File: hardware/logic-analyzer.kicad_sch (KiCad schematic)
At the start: 93 parts, among them J1 USB_C_Receptacle, J2 Conn_02x20, J3 Conn_02x04, J4 Conn_02x15, SW1 SW_Push, SW2 SW_Push, U1 CH32H417MxUx, U16 TPD4EUSB30, U2 Opamp_Dual, U22 TPD4EUSB30, U23 TPD4EUSB30, U3 CH9441P, U4 XC6206PxxxMR, Y1 25MHz 20pF

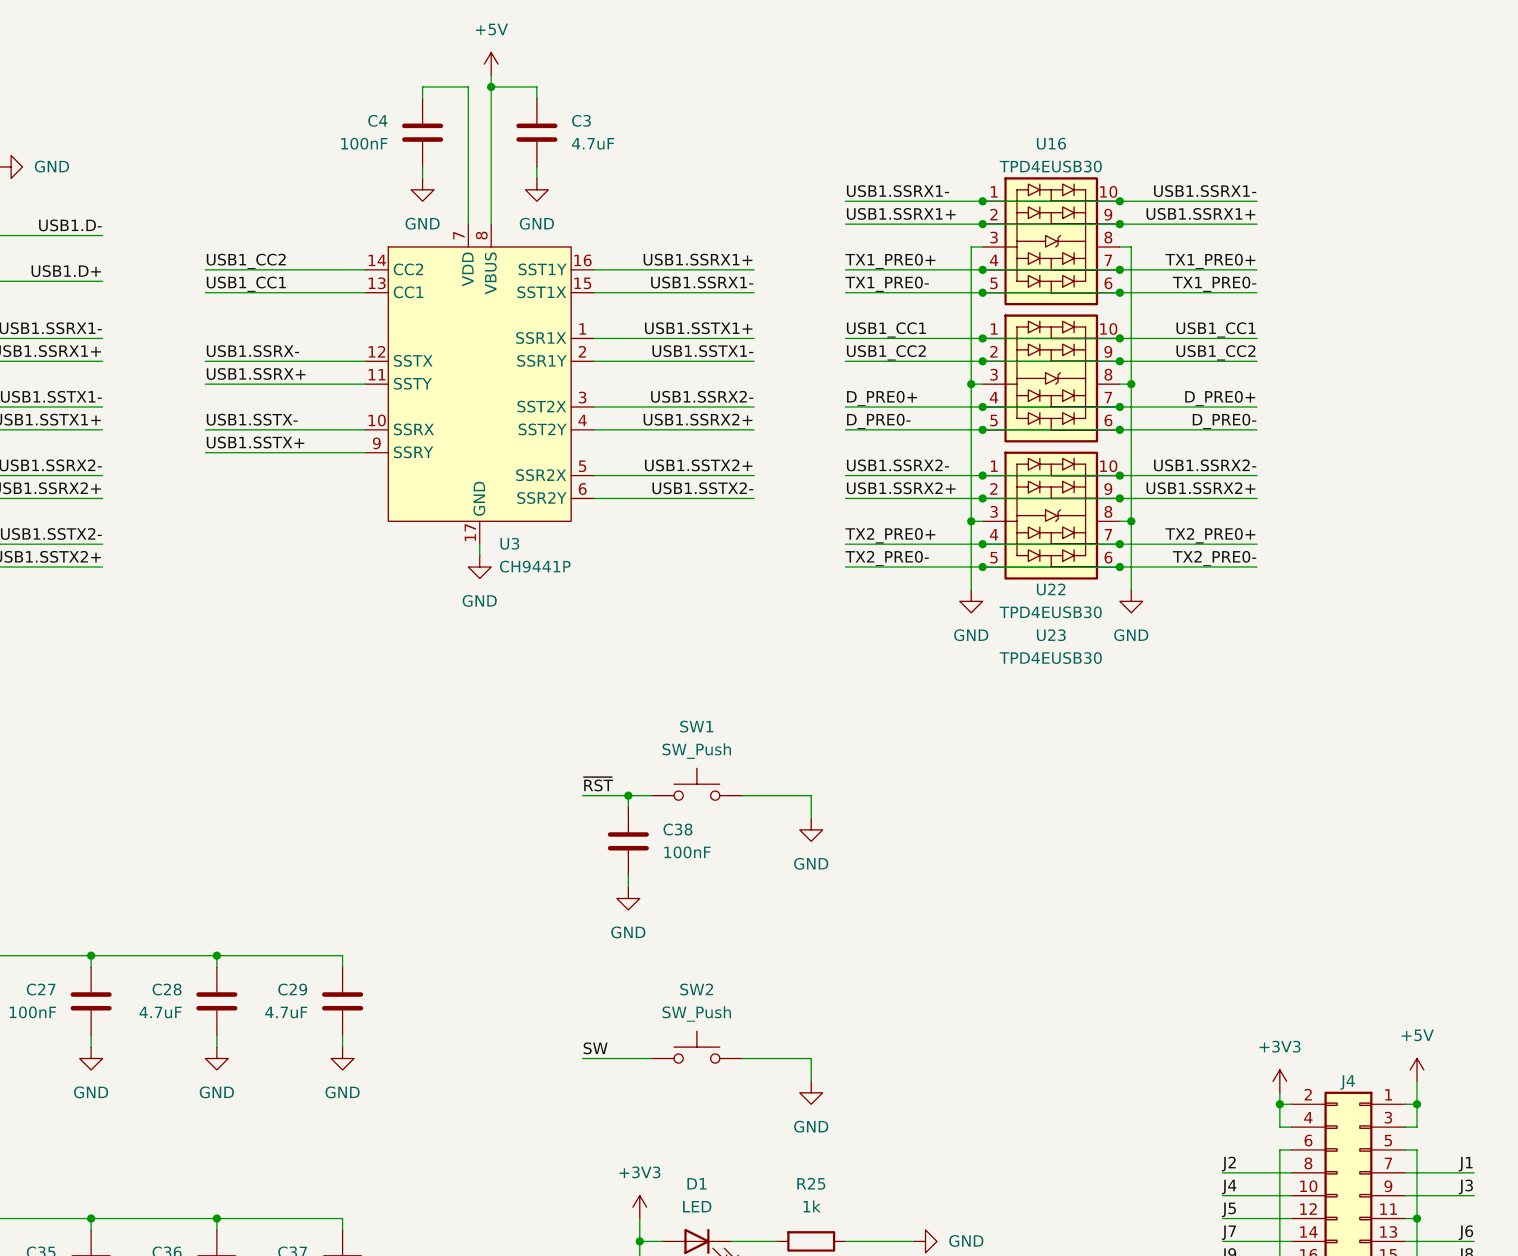
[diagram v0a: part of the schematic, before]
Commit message: Change CH9441P into something available
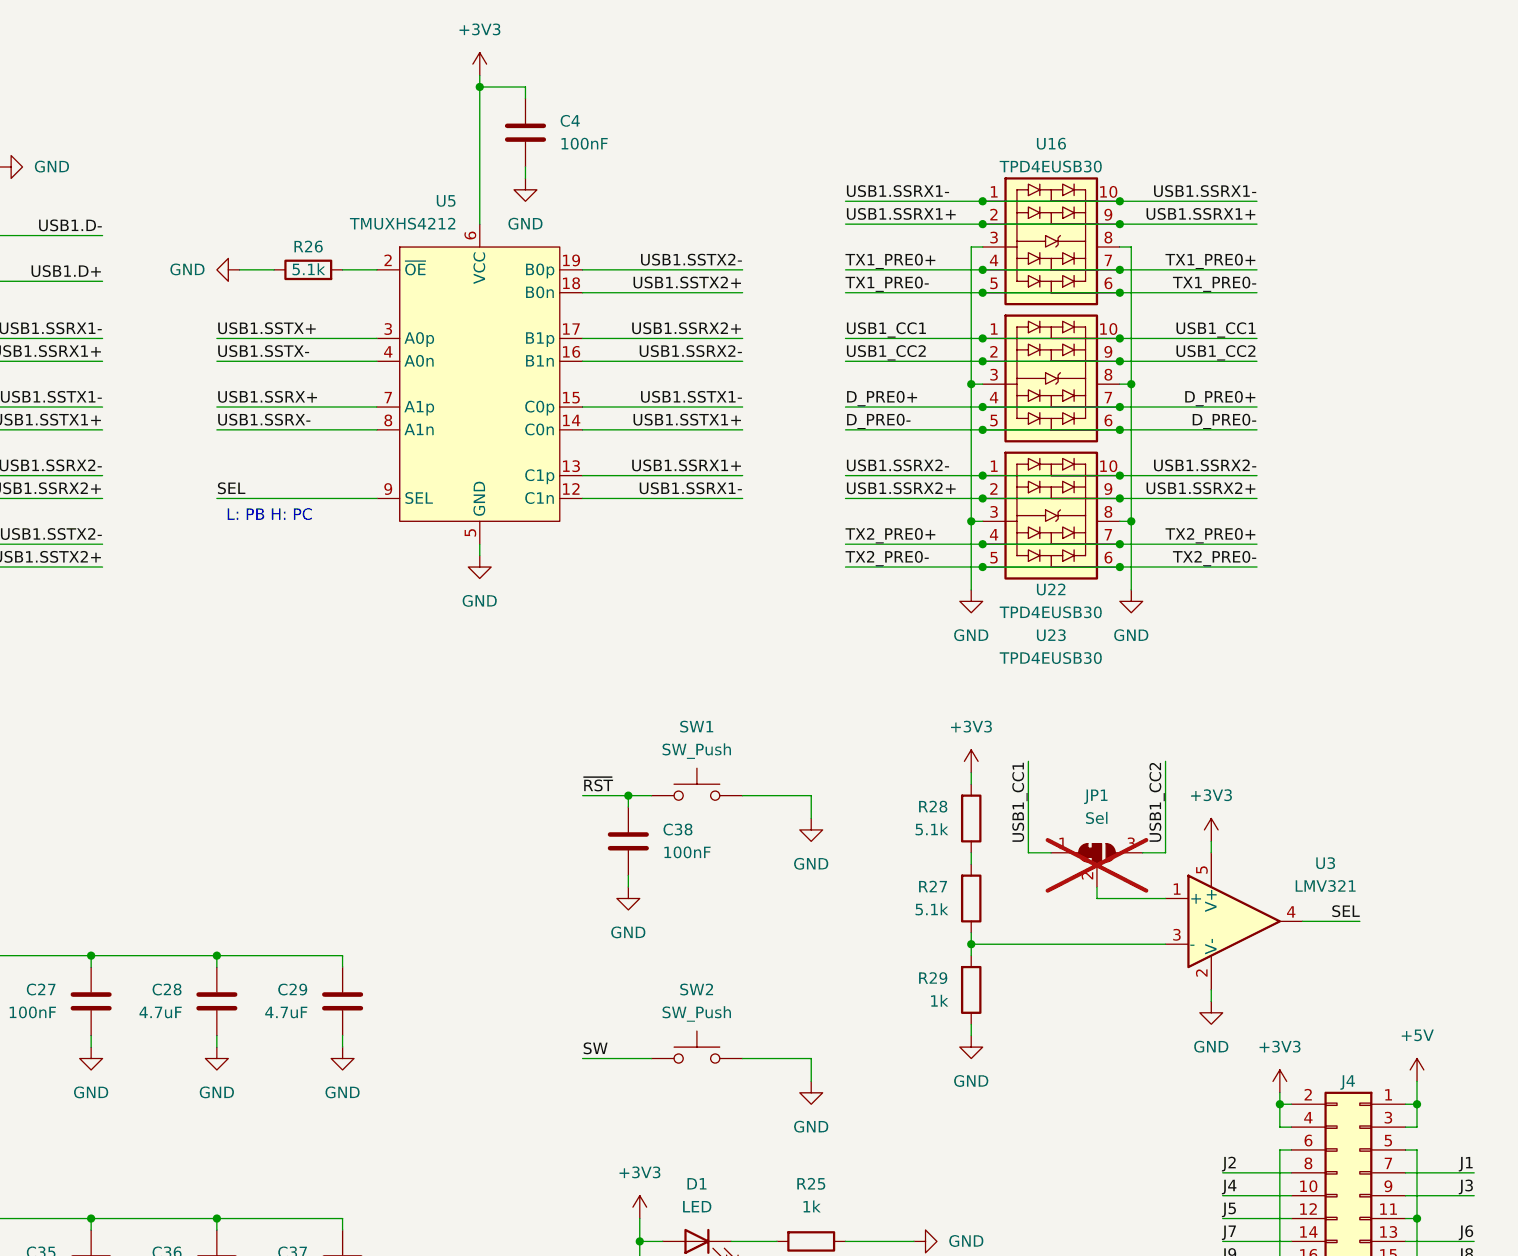
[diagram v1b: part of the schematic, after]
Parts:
- removed C3: 4.7uF, Capacitor_SMD:C_0402_1005Metric, symbol Device:C
- removed U3: CH9441P, Package_DFN_QFN:QFN-16-1EP_3x3mm_P0.5mm_EP1.75x1.75mm_ThermalVias, symbol logic-analyzer:CH9441P
- added JP1: Sel, Jumper:SolderJumper-3_P1.3mm_Bridged12_RoundedPad1.0x1.5mm, symbol Jumper:SolderJumper_3_Bridged12
- added R26, R27, R28: 5.1k, Resistor_SMD:R_0402_1005Metric, symbol Device:R
- added R29: 1k, Resistor_SMD:R_0402_1005Metric, symbol Device:R
- added U3: LMV321, Package_TO_SOT_SMD:SOT-353_SC-70-5, symbol Amplifier_Operational:LMV321
- added U5: TMUXHS4212, Package_DFN_QFN:DHVQFN-20-1EP_2.5x4.5mm_P0.5mm_EP1x3mm, symbol logic-analyzer:TMUXHS4212
- R23, R24, R25: footprint Resistor_SMD:R_0402_1005Metric_Pad0.72x0.64mm_HandSolder -> Resistor_SMD:R_0402_1005Metric
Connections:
- net +3V3: now also C4.1, R28.2, U3.5 (V+), U5.1 (RSVD1), U5.10 (RSVD2), U5.6 (VCC)
- net GND: now also R26.1, R29.1, U3.2 (V-), U5.11 (GND), U5.20 (GND), U5.21 (GND), U5.5 (GND)
- net USB1.SSRX+: now also U5.7 (A1p)
- net USB1.SSRX-: now also U5.8 (A1n)
- net USB1.SSRX1+: now also U5.13 (C1p)
- net USB1.SSRX1-: now also U5.12 (C1n)
- net USB1.SSRX2+: now also U5.17 (B1p)
- net USB1.SSRX2-: now also U5.16 (B1n)
- net USB1.SSTX+: now also U5.3 (A0p)
- net USB1.SSTX-: now also U5.4 (A0n)
- net USB1.SSTX1+: now also U5.14 (C0n)
- net USB1.SSTX1-: now also U5.15 (C0p)
- net USB1.SSTX2+: now also U5.18 (B0n)
- net USB1.SSTX2-: now also U5.19 (B0p)
- net USB1_CC1: now also JP1.1 (A)
- net USB1_CC2: now also JP1.3 (B)
- new net: JP1.2 (C), U3.1 (+)
- new net: R26.2, U5.2 (~{OE})
- new net: R27.2, R28.1
- new net: R27.1, R29.2, U3.3 (-)
- new net SEL: U3.4, U5.9 (SEL)
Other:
- note added: "L: PB H: PC"
- moved on the sheet: C4

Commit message: Readme
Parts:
- added TP1, TP2, TP3, TP4: TestPoint_Probe, TestPoint:TestPoint_Pad_D1.5mm, symbol Connector:TestPoint_Probe
- R18, R19: LCSC Part # C2906860 -> C106232
- R21, R22, R26, R27, R28: LCSC Part # C2906874 -> C105872
- R23, R24, R25, R29: LCSC Part # C2906864 -> C106235
- R97, R98: LCSC Part # C53454336 -> C54920775
- U1: LCSC Part # (none) -> C54973456
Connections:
- net +3V3: now also TP3.1
- net GND: now also TP4.1
- net USB1.D+: now also TP1.1
- net USB1.D-: now also TP2.1

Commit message: Update
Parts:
- removed C22: 100nF, Capacitor_SMD:C_0402_1005Metric, symbol Device:C
- removed R17: 220R, Resistor_SMD:R_0402_1005Metric, symbol Device:R
- removed U2: Opamp_Dual, Package_SO:VSSOP-8_2.3x2mm_P0.5mm, symbol Device:Opamp_Dual
- added R30, R31, R32: 100R, Resistor_SMD:R_0402_1005Metric, symbol Device:R
- C1, C2: MPN (none) -> GCM1555C1H330JA16J
- C10, C11, C12, C13, C14, C15, C16, C17, C18, C19, C20, C5, C6, C7, C8, C9: MPN (none) -> VJ0402A150JXAAC
- C21, C23, C24, C25, C26, C27, C30, C31, C32, C34, C35, C358, C359, C36, C360, C361, C38, C4: LCSC Part # C110251 -> C60474; MPN (none) -> CC0402KRX7R7BB104
- C28, C29, C33, C37, C39, C40: LCSC Part # C7472956 -> C51933306; MPN (none) -> GRM155R60G475ME87D
- D1, D2, D3: LCSC Part # C20613596 -> C51933306
- J2: footprint Connector_PinSocket_1.27mm:PinSocket_2x20_P1.27mm_Horizontal -> Connector_PinHeader_1.27mm:PinHeader_2x20_P1.27mm_Horizontal
- J3: footprint Connector_PinSocket_1.27mm:PinSocket_2x04_P1.27mm_Horizontal -> Connector_PinHeader_1.27mm:PinHeader_2x04_P1.27mm_Horizontal
- R1, R10, R11, R12, R13, R14, R15, R16, R2, R3, R4, R5, R6, R7, R8, R9: LCSC Part # C2906864 -> C106235; MPN (none) -> RC0402FR-071KL
- R18, R19: MPN (none) -> MCS04020C1000FE000
- R20: value 220R -> 100R; LCSC Part # C25091 -> C106232; MPN (none) -> MCS04020C1000FE000
- R21, R22, R26, R27, R28: MPN (none) -> AC0402FR-075K1L
- R23, R24, R25, R29: MPN (none) -> RC0402FR-071KL
- R97, R98: MPN (none) -> RC0402FR-072R2L
- RN1, RN2, RN3, RN4: MPN (none) -> EXB-V8V104JV
- U1: MPN (none) -> CH32H417MEU6
- U16, U22, U23: MPN (none) -> TPD4EUSB30DQAR
- U3: MPN (none) -> LMV321IDCKT
- U4: MPN (none) -> XC6206P332MR-G
- U5: MPN (none) -> TMUXHS4212RKSR
- Y1: LCSC Part # C252274 -> C37635326; MPN (none) -> XT1220HJRGX25M00E
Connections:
- net +1V8: now also J2.27 (Pin_27), J2.37 (Pin_37); no longer J2.13 (Pin_13), J2.3 (Pin_3)
- net +3V3: now also J2.17 (Pin_17), J2.7 (Pin_7); no longer J2.23 (Pin_23), J2.33 (Pin_33)
- net +5V: no longer J4.3 (Pin_3)
- net A0: now also R18.2, R30.1
- net A1: now also R19.2, R20.1
- net ACH0: now also J3.6 (Pin_6); no longer J3.4 (Pin_4)
- net ACH1: now also J3.2 (Pin_2); no longer J3.8 (Pin_8)
- net CH0: now also J2.38 (Pin_38); no longer J2.4 (Pin_4)
- net CH1: now also J2.36 (Pin_36); no longer J2.6 (Pin_6)
- net CH10: now also J2.14 (Pin_14); no longer J2.28 (Pin_28)
- net CH11: now also J2.12 (Pin_12); no longer J2.30 (Pin_30)
- net CH12: now also J2.8 (Pin_8); no longer J2.34 (Pin_34)
- net CH13: now also J2.6 (Pin_6); no longer J2.36 (Pin_36)
- net CH14: now also J2.4 (Pin_4); no longer J2.38 (Pin_38)
- net CH15: now also J2.2 (Pin_2); no longer J2.40 (Pin_40)
- net CH2: now also J2.34 (Pin_34); no longer J2.8 (Pin_8)
- net CH3: now also J2.32 (Pin_32); no longer J2.10 (Pin_10)
- net CH4: now also J2.28 (Pin_28); no longer J2.14 (Pin_14)
- net CH5: now also J2.26 (Pin_26); no longer J2.16 (Pin_16)
- net CH6: now also J2.24 (Pin_24); no longer J2.18 (Pin_18)
- net CH7: now also J2.22 (Pin_22); no longer J2.20 (Pin_20)
- net CH8: now also J2.18 (Pin_18); no longer J2.24 (Pin_24)
- net CH9: now also J2.16 (Pin_16); no longer J2.26 (Pin_26)
- net GND: now also J2.10 (Pin_10), J2.13 (Pin_13), J2.20 (Pin_20), J2.23 (Pin_23), J2.3 (Pin_3), J2.30 (Pin_30), J2.33 (Pin_33), J2.40 (Pin_40), J3.4 (Pin_4), J3.8 (Pin_8), R31.2, R32.2; no longer J2.12 (Pin_12), J2.17 (Pin_17), J2.2 (Pin_2), J2.22 (Pin_22), J2.27 (Pin_27), J2.32 (Pin_32), J2.37 (Pin_37), J2.7 (Pin_7), J3.2 (Pin_2), J3.6 (Pin_6), J4.5 (Pin_5), R20.2
- net USB1.D+: now also J4.3 (Pin_3)
- net USB1.D-: now also J4.5 (Pin_5)
- new net: R20.2, R32.1
- new net: R30.2, R31.1
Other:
- moved on the sheet: R18, R19

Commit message: Stencil
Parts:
- added H1, H2: MountingHole, logic-analyzer:Icy Electronics Logo, symbol Mechanical:MountingHole
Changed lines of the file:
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@@
 	)
 	(symbol
+		(lib_id "Mechanical:MountingHole")
+		(at 400.05 260.35 0)
+		(unit 1)
+		(body_style 1)
+		(exclude_from_sim no)
+		(in_bom no)
+		(on_board yes)
+		(in_pos_files yes)
+		(dnp no)
+		(fields_autoplaced yes)
+		(property "Reference" "H1"
+			(at 402.59 259.0799 0)
+			(hide yes)
+			(show_name no)
+			(do_not_autoplace no)
+			(effects
+				(font
+					(size 1.27 1.27)
+				)
+				(justify left)
+			)
+		)
+		(property "Value" "MountingHole"
+			(at 402.59 261.6199 0)
+			(hide yes)
+			(show_name no)
+			(do_not_autoplace no)
+			(effects
+				(font
+					(size 1.27 1.27)
+				)
+				(justify left)
+			)
+		)
+		(property "Footprint" "logic-analyzer:Icy Electronics Logo"
+			(at 400.05 260.35 0)
+			(hide yes)
+			(show_name no)
+			(do_not_autoplace no)
+			(effects
+				(font
+					(size 1.27 1.27)
+				)
+			)
+		)
+		(property "Datasheet" ""
+			(at 400.05 260.35 0)
+			(hide yes)
+			(show_name no)
+			(do_not_autoplace no)
+			(effects
+				(font
+					(size 1.27 1.27)
+				)
+			)
+		)
+		(property "Description" "Mounting Hole without connection"
+			(at 400.05 260.35 0)
+			(hide yes)
+			(show_name no)
+			(do_not_autoplace no)
+			(effects
+				(font
+					(size 1.27 1.27)
+				)
+			)
+		)
+		(instances
+			(project "logic-analyzer"
+				(path "/5f684d88-c692-47c7-8c9f-30135288a837"
+					(reference "H1")
+					(unit 1)
+				)
+			)
+		)
+	)
+	(symbol
 		(lib_id "power:GND")
 		(at 185.42 133.35 0)
@@
 					(unit 1)
 				)
+			)
+		)
+	)
+	(symbol
+		(lib_id "Mechanical:MountingHole")
+		(at 391.16 260.35 0)
+		(unit 1)
+		(body_style 1)
+		(exclude_from_sim no)
+		(in_bom no)
+		(on_board yes)
+		(in_pos_files yes)
+		(dnp no)
+		(fields_autoplaced yes)
+		(property "Reference" "H2"
+			(at 393.7 259.0799 0)
+			(hide yes)
+			(show_name no)
+			(do_not_autoplace no)
+			(effects
+				(font
+					(size 1.27 1.27)
+				)
+				(justify left)
+			)
+		)
+		(property "Value" "MountingHole"
+			(at 393.7 261.6199 0)
+			(hide yes)
+			(show_name no)
+			(do_not_autoplace no)
+			(effects
+				(font
+					(size 1.27 1.27)
+				)
+				(justify left)
+			)
+		)
+		(property "Footprint" "logic-analyzer:Icy Electronics Logo"
+			(at 391.16 260.35 0)
+			(hide yes)
+			(show_name no)
+			(do_not_autoplace no)
+			(effects
+				(font
+					(size 1.27 1.27)
+				)
+			)
+		)
+		(property "Datasheet" ""
+			(at 391.16 260.35 0)
+			(hide yes)
+			(show_name no)
+			(do_not_autoplace no)
+			(effects
+				(font
+					(size 1.27 1.27)
+				)
+			)
+		)
+		(property "Description" "Mounting Hole without connection"
+			(at 391.16 260.35 0)
+			(hide yes)
+			(show_name no)
+			(do_not_autoplace no)
+			(effects
+				(font
+					(size 1.27 1.27)
+				)
+			)
+		)
+		(instances
+			(project "logic-analyzer"
+				(path "/5f684d88-c692-47c7-8c9f-30135288a837"
+					(reference "H2")
+					(unit 1)
+				)

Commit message: General improvements
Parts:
- removed R31, R32: 100R, Resistor_SMD:R_0402_1005Metric, symbol Device:R
- removed TP1, TP2, TP3, TP4: TestPoint_Probe, TestPoint:TestPoint_Pad_D1.5mm, symbol Connector:TestPoint_Probe
- removed U4: XC6206PxxxMR, Package_TO_SOT_SMD:SOT-23-3, symbol Regulator_Linear:XC6206PxxxMR
- added C41: 4.7uF, Capacitor_SMD:C_0402_1005Metric, symbol Device:C
- added J5: Conn_02x15, Connector_PinHeader_2.54mm:PinHeader_2x15_P2.54mm_Vertical, symbol Connector_Generic:Conn_02x15_Odd_Even
- added U2: AMS1117-3.3, Package_TO_SOT_SMD:SOT-89-3, symbol Regulator_Linear:AMS1117-3.3
- C28, C29, C33, C37, C39, C40: LCSC Part # C51933306 -> C380302
- J4: footprint Connector_PinSocket_2.54mm:PinSocket_2x15_P2.54mm_Vertical -> Connector_PinHeader_2.54mm:PinHeader_2x15_P2.54mm_Vertical
- R1, R10, R11, R12, R13, R14, R15, R16, R2, R23, R24, R25, R29, R3, R4, R5, R6, R7, R8, R9: LCSC Part # C106235 -> C11702
- SW1, SW2: LCSC Part # C2888427 -> C2888428
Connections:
- net +3V3: now also J4.1 (Pin_1), J4.3 (Pin_3), C41.1, J5.30 (Pin_30), U2.2 (VO); no longer J4.2 (Pin_2), J4.4 (Pin_4)
- net +5V: now also J4.2 (Pin_2), U2.3 (VI); no longer J4.1 (Pin_1)
- net GND: now also J4.12 (Pin_12), J4.17 (Pin_17), J4.26 (Pin_26), J4.29 (Pin_29), J4.5 (Pin_5), R20.2, R30.2, C41.2, J5.12 (Pin_12), J5.17 (Pin_17), J5.2 (Pin_2), J5.26 (Pin_26), J5.29 (Pin_29), J5.5 (Pin_5), U2.1 (GND); no longer J4.11 (Pin_11), J4.18 (Pin_18), J4.25 (Pin_25), J4.30 (Pin_30), J4.6 (Pin_6)
- net J1: now also J4.8 (Pin_8); no longer J4.7 (Pin_7)
- net J10: now also J4.18 (Pin_18); no longer J4.17 (Pin_17)
- net J11: now also J4.20 (Pin_20); no longer J4.19 (Pin_19)
- net J12: now also J4.19 (Pin_19); no longer J4.20 (Pin_20)
- net J13: now also J4.22 (Pin_22); no longer J4.21 (Pin_21)
- net J14: now also J4.21 (Pin_21); no longer J4.22 (Pin_22)
- net J15: now also J4.24 (Pin_24); no longer J4.23 (Pin_23)
- net J16: now also J4.23 (Pin_23); no longer J4.24 (Pin_24)
- net J17: now also J4.25 (Pin_25); no longer J4.26 (Pin_26)
- net J18: now also J4.28 (Pin_28); no longer J4.27 (Pin_27)
- net J19: now also J4.27 (Pin_27); no longer J4.28 (Pin_28)
- net J2: now also J4.7 (Pin_7); no longer J4.8 (Pin_8)
- net J20: now also J4.30 (Pin_30); no longer J4.29 (Pin_29)
- net J3: now also J4.10 (Pin_10); no longer J4.9 (Pin_9)
- net J4: now also J4.9 (Pin_9); no longer J4.10 (Pin_10)
- net J5: now also J4.11 (Pin_11); no longer J4.12 (Pin_12)
- net J6: now also J4.14 (Pin_14); no longer J4.13 (Pin_13)
- net J7: now also J4.13 (Pin_13); no longer J4.14 (Pin_14)
- net J8: now also J4.16 (Pin_16); no longer J4.15 (Pin_15)
- net J9: now also J4.15 (Pin_15); no longer J4.16 (Pin_16)
- net USB1.D+: now also J4.4 (Pin_4); no longer J4.3 (Pin_3)
- net USB1.D-: now also J4.6 (Pin_6); no longer J4.5 (Pin_5)
- net J36: now reaches U1.30 (PE14)
- net J36: now also J5.20 (Pin_20)
- net J35: now reaches U1.31 (PE15)
- net J35: now also J5.19 (Pin_19)
- net J34: now reaches U1.32 (PB10)
- net J34: now also J5.18 (Pin_18)
- net J33: now reaches U1.33 (PB11)
- net J33: now also J5.16 (Pin_16)
- net J32: now reaches U1.36 (PB12)
- net J32: now also J5.15 (Pin_15)
- net J31: now reaches U1.37 (PB13)
- net J31: now also J5.14 (Pin_14)
- net J30: now reaches U1.38 (PB14)
- net J30: now also J5.13 (Pin_13)
- net J29: now reaches U1.39 (PD10)
- net J29: now also J5.11 (Pin_11)
- net J28: now reaches U1.40 (PD11)
- net J28: now also J5.10 (Pin_10)
- net J27: now reaches U1.41 (PD12)
- net J27: now also J5.9 (Pin_9)
- net J26: now reaches U1.42 (PD13)
- net J26: now also J5.8 (Pin_8)
- net J25: now reaches U1.43 (PD14)
- net J25: now also J5.7 (Pin_7)
- net J24: now reaches U1.44 (PD15)
- net J24: now also J5.6 (Pin_6)
- net J22: now reaches U1.46 (PF1)
- net J22: now also J5.3 (Pin_3)
- net J21: now reaches U1.47 (PF2)
- net J21: now also SW2.2, J5.1 (Pin_1)
- net J42: now reaches U1.60 (PA14)
- net J42: now also J5.27 (Pin_27)
- net J43: now reaches U1.61 (PA15)
- net J43: now also J5.28 (Pin_28)
- net J41: now reaches U1.62 (PC10)
- net J41: now also J5.25 (Pin_25)
- net J40: now reaches U1.63 (PC11)
- net J40: now also J5.24 (Pin_24)
- net J39: now reaches U1.64 (PC12)
- net J39: now also J5.23 (Pin_23)
- net J37: now reaches U1.65 (PD0)
- net J37: now also J5.21 (Pin_21)
- net J38: now reaches U1.66 (PD1)
- net J38: now also J5.22 (Pin_22)
- net SW renamed J23
- net J23: now also J5.4 (Pin_4); no longer SW2.2
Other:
- moved on the sheet: C39
